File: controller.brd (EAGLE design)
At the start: 160 x 100 mm, 45 parts, among them IC1 MC34063AD, IC2 7805T, IC3 MEGA8-AI, Q1 IRF840, Q2 32768Hz, Q3 4MHz, T1 BC857, U1 DS1307Z

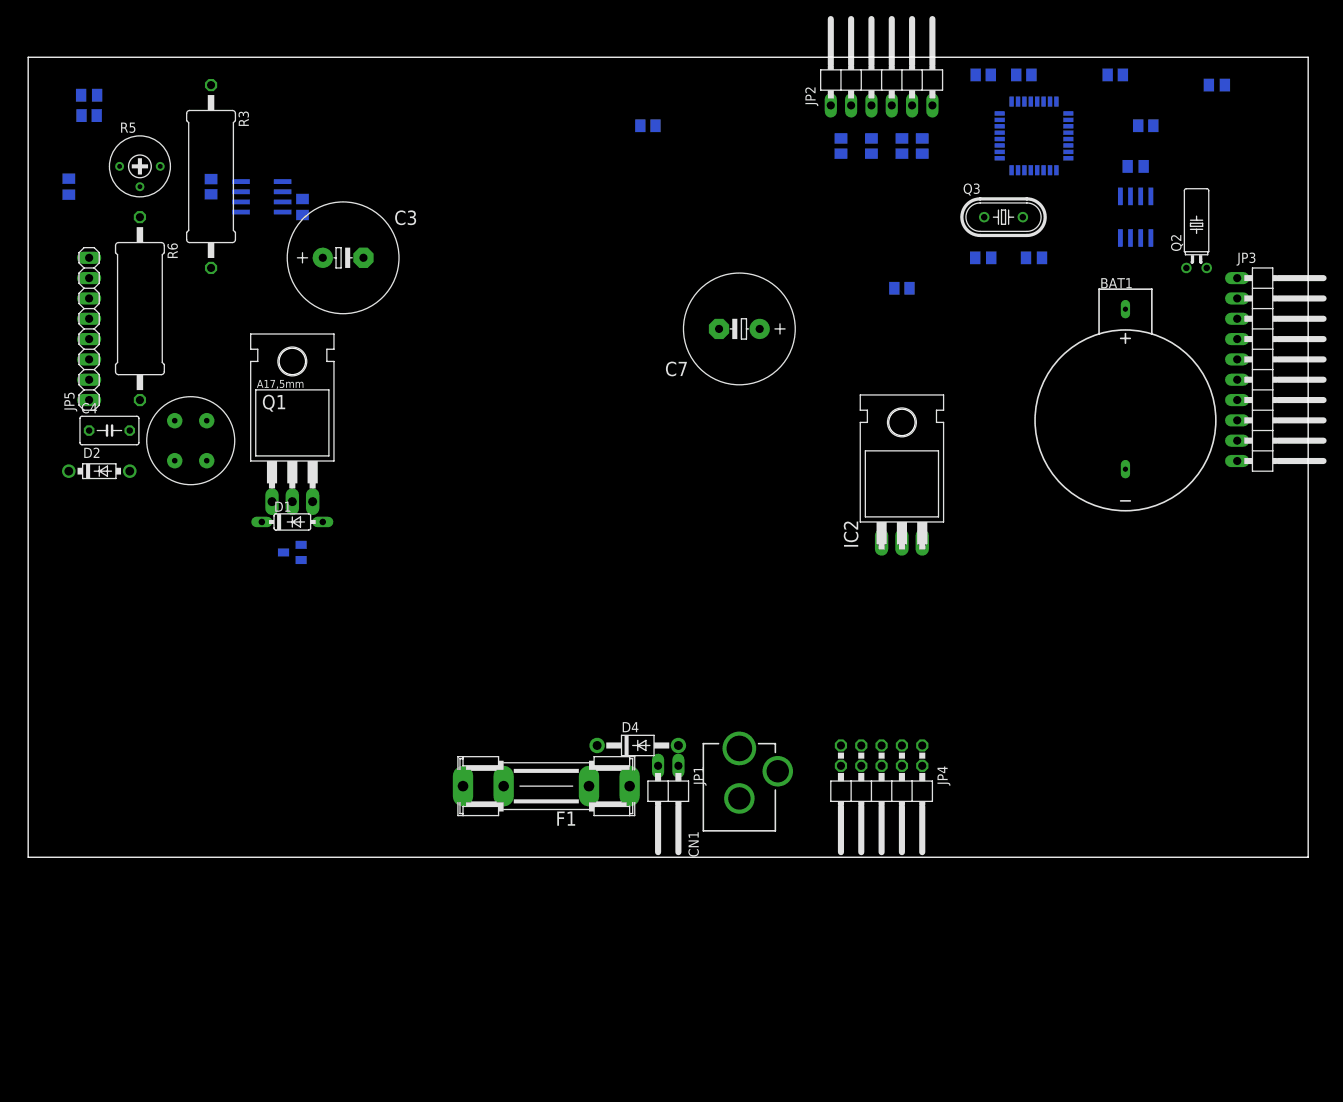
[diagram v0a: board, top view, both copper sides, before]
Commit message: Dimensions defined
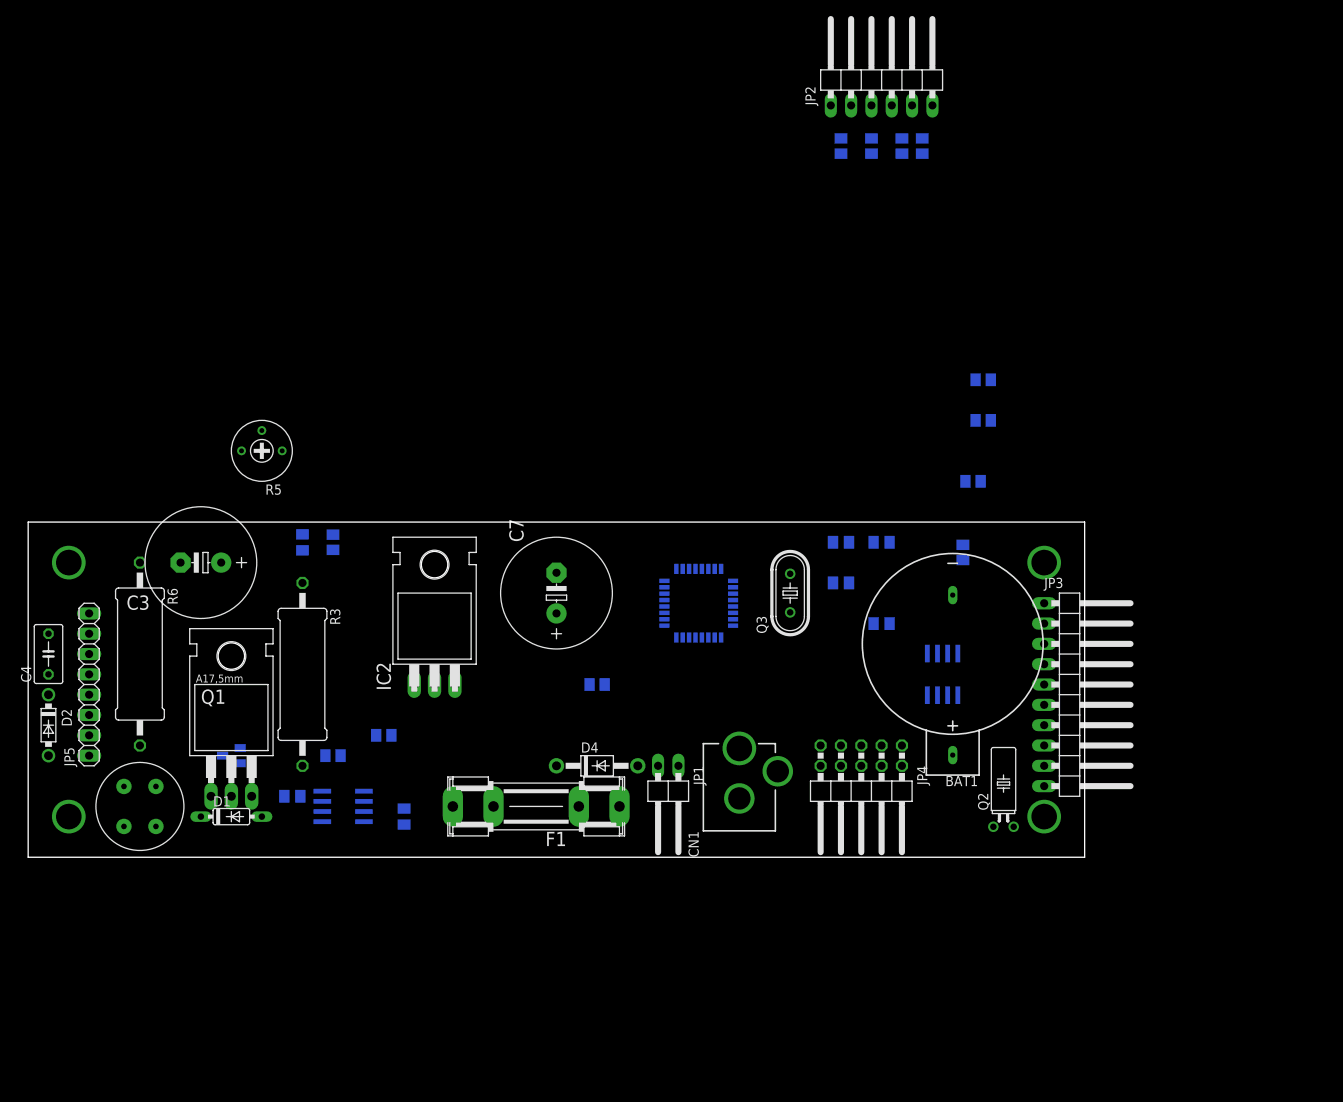
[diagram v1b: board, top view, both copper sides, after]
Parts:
- moved C2 91.2 mm to (33.0, 7.62)
- moved R1 83.0 mm to (44.5, 15.2)
- moved C1 77.3 mm to (47.0, 5.08)
- moved IC1 76.9 mm to (39.4, 6.35)
- moved Q2 73.9 mm to (121.9, 3.81)
- moved R2 72.7 mm to (38.1, 12.7), turned to 180 degrees
- moved IC3 71.9 mm to (83.8, 31.8)
- moved C5 70.9 mm to (106.7, 39.4), turned to 180 degrees
- moved C10 65.4 mm to (106.7, 29.2)
- moved R3 63.3 mm to (34.3, 22.9)
- moved R15 62.5 mm to (71.1, 21.6)
- moved U1 62.0 mm to (114.3, 22.9)
- moved R4 61.4 mm to (38.1, 39.4), turned to 90 degrees
- moved IC2 61.1 mm to (50.8, 31.8)
- moved R12 58.0 mm to (116.8, 38.1), turned to 90 degrees
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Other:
- board size 160 x 100 mm -> 132.1 x 41.9 mm

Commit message: Update
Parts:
- removed JP1: POWER +12V, pinhead:1X02/90
- removed JP3: EXTERNAL, pinhead:1X10/90
- moved C3 48.3 mm to (20.3, -11.4)
- moved JP2 47.2 mm to (78.7, 59.7)
- moved R10 47.2 mm to (83.8, 50.8)
- moved R8 47.2 mm to (77.5, 50.8)
- moved R9 47.2 mm to (81.3, 50.8)
- moved R7 46.5 mm to (74.9, 50.8)
- moved R5 43.0 mm to (15.2, 10.2)
- moved C6 34.9 mm to (53.3, 10.2), turned to 270 degrees
- moved R4 31.9 mm to (50.8, 10.2)
- moved D4 18.9 mm to (88.9, 17.8)
- moved R14 14.5 mm to (108.0, 50.8)
- moved R13 13.7 mm to (108.0, 47.0)
- moved R1 13.3 mm to (40.6, 2.54)
- moved Q1 11.5 mm to (24.1, 25.4)
- moved U$1 10.9 mm to (24.1, 10.2)
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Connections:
- removed net N$21: IC3.30, JP3.2
- removed net N$22: IC3.31, JP3.3
- removed net N$33: IC3.11, JP3.9
- removed net N$34: IC3.10, JP3.8
- removed net N$35: IC3.9, JP3.7
- removed net N$36: IC3.2, JP3.6
- removed net N$37: IC3.1, JP3.5
- net +5V: no longer JP3.1
- net GND: no longer JP1.1, JP3.10, JP3.4
- net N$29: no longer JP1.2

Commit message: .
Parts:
- added C11: 100nF, SparkFun-Passives:0805
- C1: value 200p -> 200pF; device resistor:C0805K -> SparkFun-Passives:0805
- C10, C2, C5, C6: value 100n -> 100nF; device resistor:C0805K -> SparkFun-Passives:0805
- C8, C9: device rcl:C0805K -> SparkFun-Passives:0805
- R1: value 1K -> 1k; device resistor:M0805 -> SparkFun-Passives:0805
- R10, R11, R12, R13, R14, R4, R7, R8, R9: value 10K -> 10k; device resistor:M0805 -> SparkFun-Passives:0805
- R15: value 1K -> 10k; device resistor:M0805 -> SparkFun-Passives:0805
- R3, R6: device resistor:0617/22 -> SparkFun-Passives:AXIAL-0.8
- moved C5 80.2 mm to (33.0, 7.62), flipped to the top
- moved C6 44.6 mm to (8.89, 6.35), flipped to the top, turned to 0 degrees
- moved R12 43.1 mm to (74.9, 48.3), flipped to the top, turned to 0 degrees
- moved R14 40.7 mm to (67.3, 48.3), flipped to the top, turned to 0 degrees
- moved R4 37.4 mm to (14.0, 3.81), flipped to the top, turned to 0 degrees
- moved R13 36.9 mm to (71.1, 48.3), flipped to the top, turned to 0 degrees
- moved R11 29.5 mm to (78.7, 48.3), flipped to the top, turned to 0 degrees
- moved C10 28.7 mm to (78.7, 22.9), flipped to the top, turned to 0 degrees
- moved R15 27.7 mm to (63.5, 48.3), flipped to the top
- moved C8 24.3 mm to (83.8, 22.9), flipped to the top
- moved R1 22.9 mm to (17.8, 3.81), flipped to the top
- moved C2 21.6 mm to (14.0, 1.27), flipped to the top, turned to 0 degrees
- moved R7 19.2 mm to (94.0, 48.3), flipped to the top, turned to 0 degrees
- moved C9 17.3 mm to (87.6, 24.1), flipped to the top
- moved R8 13.0 mm to (90.2, 48.3), flipped to the top, turned to 0 degrees
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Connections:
- net +5V: now also C6.1; no longer C5.1
- net 200V: now also R6.P$2; no longer R6.2
- net GND: now also C11.1
- net N$11: now also R6.P$1; no longer R6.1
- net N$18: now also R15.2; no longer R15.1
- net N$32: now also R15.1; no longer R15.2
- net N$7: now also R3.P$2; no longer R3.2
- net N$8: now also C5.1, R3.P$1; no longer C6.1, R3.1
- net N$9: now also C11.2

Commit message: .
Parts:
- moved R14 52.1 mm to (110.5, 19.1), flipped to the bottom, turned to 90 degrees
- moved R13 51.1 mm to (113.0, 19.1), flipped to the bottom, turned to 90 degrees
- moved R12 50.0 mm to (115.6, 19.1), flipped to the bottom, turned to 90 degrees
- moved JP2 44.7 mm to (115.6, 34.3)
- moved C10 40.7 mm to (119.4, 21.6), flipped to the bottom, turned to 180 degrees
- moved R10 39.6 mm to (119.4, 33.7), flipped to the bottom, turned to 90 degrees
- moved D1 35.3 mm to (43.2, 31.8), turned to 270 degrees
- moved R9 33.8 mm to (116.8, 33.7), flipped to the bottom, turned to 90 degrees
- moved R15 28.5 mm to (78.7, 24.1), flipped to the bottom, turned to 180 degrees
- moved R8 28.2 mm to (114.3, 33.7), flipped to the bottom, turned to 90 degrees
- moved D4 27.1 mm to (62.2, 12.7)
- moved F1 23.7 mm to (49.5, 5.08)
- moved R7 23.0 mm to (111.8, 33.7), flipped to the bottom, turned to 90 degrees
- moved Q2 16.5 mm to (128.3, 19.1), turned to 180 degrees
- moved BAT1 15.3 mm to (114.3, 11.4), turned to 0 degrees
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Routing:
- net +5V: track 0.00 -> 88.9 mm
- net N$24: track 0.00 -> 65.9 mm
- net N$30: track 0.00 -> 65.0 mm
- net N$31: track 0.00 -> 62.8 mm
- net N$32: track 0.00 -> 61.3 mm
- net GND: track 0.00 -> 45.3 mm
- net N$23: track 0.00 -> 17.3 mm
- net N$28: track 0.00 -> 9.25 mm
- net N$26: track 0.00 -> 7.98 mm
- net N$27: track 0.00 -> 3.78 mm
- net N$25: track 0.00 -> 3.11 mm
- net N$3: track 0.00 -> 2.28 mm
- net N$15: track 0.00 -> 2.28 mm
- net N$14: track 0.00 -> 2.28 mm
- net N$13: track 0.00 -> 2.28 mm

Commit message: Controller
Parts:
- removed R10, R7, R8, R9: 10k, SparkFun-Passives:0805
- C1: value 200pF -> 1nF
- C3: value 10u 450V -> 10uF 450V
- C4: value 100n 450V -> 100nF 450V; device resistor:C050-035X075 -> SparkFun-Passives:CAP-PTH-LARGE
- C7: value 470u -> 470uF
- R2: device resistor:M0805 -> SparkFun-Passives:0805
- moved C7 76.2 mm to (123.2, -21.6)
- moved C6 71.0 mm to (78.1, 22.2), flipped to the bottom
- moved C5 43.8 mm to (74.3, 22.2), flipped to the bottom
- moved R1 39.2 mm to (52.7, 21.6), flipped to the bottom, turned to 90 degrees
- moved C11 38.6 mm to (108.0, 10.2), turned to 270 degrees
- moved D2 38.1 mm to (36.2, 34.3), turned to 0 degrees
- moved C3 34.3 mm to (19.1, 22.9), turned to 0 degrees
- moved R11 32.3 mm to (108.0, 15.2), turned to 270 degrees
- moved T1 29.2 mm to (49.5, 21.6), flipped to the bottom, turned to 270 degrees
- moved IC2 25.5 mm to (76.2, 29.2)
- moved Q1 25.4 mm to (49.5, 24.1)
- moved R2 23.6 mm to (53.3, 5.08), turned to 90 degrees
- moved R3 20.8 mm to (47.0, 6.35), turned to 180 degrees
- moved F1 19.8 mm to (63.5, 19.1), turned to 90 degrees
- moved R4 19.7 mm to (33.7, 5.08), flipped to the bottom, turned to 90 degrees
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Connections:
- net +5V: no longer R10.2, R7.2, R8.2, R9.2
- net N$13: no longer R8.1
- net N$14: no longer R9.1
- net N$15: no longer R10.1
- net N$3: no longer R7.1
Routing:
- net GND: track 45.3 -> 289.2 mm
- net N$8: track 0.00 -> 56.1 mm
- net +5V: track 88.9 -> 144.2 mm
- net N$24: track 65.9 -> 118.8 mm
- net N$31: track 62.8 -> 115.6 mm
- net N$30: track 65.0 -> 117.2 mm
- net 200V: track 0.00 -> 43.4 mm
- net N$4: track 0.00 -> 33.2 mm
- net N$10: track 0.00 -> 32.6 mm, vias 0 -> 1
- net N$7: track 0.00 -> 27.5 mm
- net N$2: track 0.00 -> 26.2 mm
- net N$20: track 0.00 -> 25.2 mm, vias 0 -> 1
- net N$32: track 61.3 -> 86.0 mm
- net N$15: track 2.28 -> 20.9 mm
- net N$29: track 0.00 -> 18.5 mm
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- added copper zone on layer 16, net N$22

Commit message: .
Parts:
- moved Q2 3.59 mm to (125.7, 21.6), turned to 0 degrees
- moved R15 2.84 mm to (86.4, 33.0)
- moved C11 2.84 mm to (106.7, 12.7), turned to 90 degrees
- moved R11 1.80 mm to (106.7, 16.5), turned to 90 degrees
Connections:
- net N$25: now also Q2.1; no longer Q2.2
- net N$26: now also Q2.2; no longer Q2.1
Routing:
- net N$18: track 0.00 -> 34.0 mm, vias 0 -> 1
- net N$19: track 0.00 -> 26.5 mm, vias 0 -> 1
- net N$9: track 0.00 -> 26.1 mm
- net GND: track 289.2 -> 313.5 mm
- net N$32: track 86.0 -> 101.9 mm
- net +5V: track 144.2 -> 155.6 mm
- net N$26: track 7.98 -> 6.18 mm
- net N$20: track 25.2 -> 26.3 mm

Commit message: Controller prototype finished
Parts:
- removed C7: 470uF, resistor:E5-13
- added C12: 100uF, rcl:E3,5-8
- R5: value 200K -> (none); device resistor:RTRIM3339P -> rcl:RTRIM64Z
- moved C11 6.75 mm to (102.2, 17.8)
- moved R11 6.29 mm to (102.2, 21.0)
- moved R13 2.54 mm to (112.4, 15.2)
- moved R5 2.54 mm to (27.9, 7.62)
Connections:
- net +5V: now also C12.+; no longer C7.+
- net GND: now also C12.-; no longer C7.-
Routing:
- net +5V: track 155.6 -> 242.3 mm, vias 0 -> 3
- net GND: track 313.5 -> 342.7 mm
- net N$12: track 3.86 -> 27.8 mm, vias 0 -> 2
- net N$16: track 3.90 -> 24.4 mm
- net N$17: track 11.8 -> 19.1 mm, vias 0 -> 2
- net N$10: track 32.6 -> 39.0 mm, vias 1 -> 2
- net N$11: track 7.93 -> 14.1 mm
- net N$9: track 26.1 -> 30.5 mm
- net N$20: track 26.3 -> 25.2 mm
- net N$19: track 26.5 -> 25.9 mm
- net N$18: track 34.0 -> 33.4 mm
- removed copper zone on layer 16, net N$22

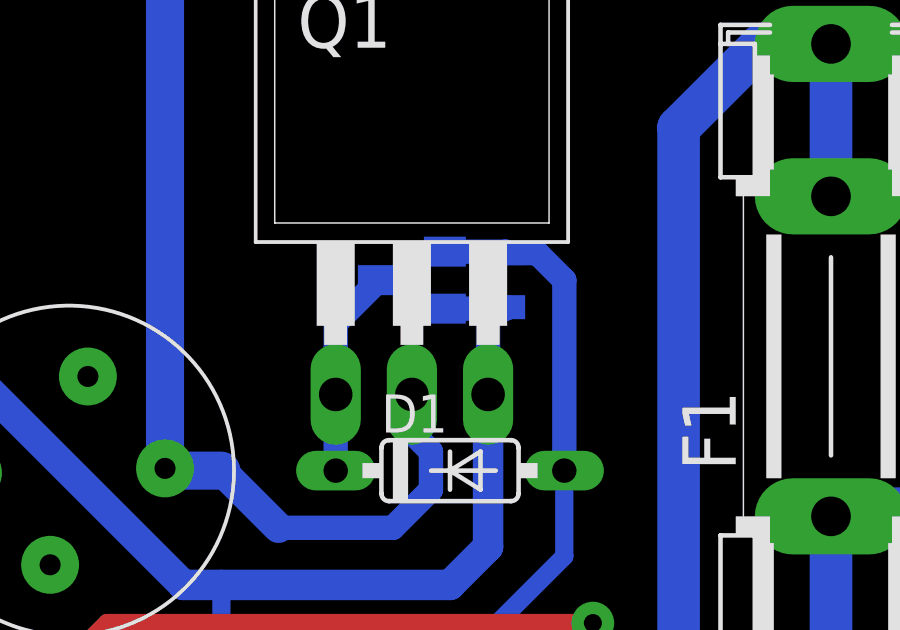
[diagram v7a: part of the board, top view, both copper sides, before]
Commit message: Correct pnp transistor pinout
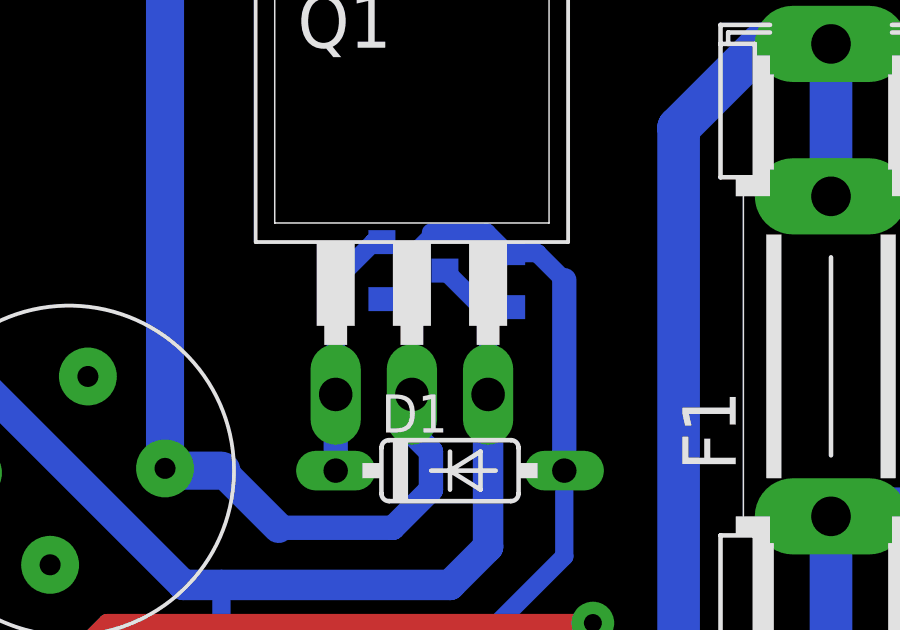
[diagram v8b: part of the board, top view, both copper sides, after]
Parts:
- removed T1: BC857, transistor:SOT23-BCE
- added Q6: BC857, SparkFun-DiscreteSemi:SOT23-3
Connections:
- net GND: now also Q6.3; no longer T1.C
- net N$1: now also Q6.2; no longer T1.E
- net N$2: now also Q6.1; no longer T1.B
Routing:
- net N$2: track 26.2 -> 30.3 mm
- net N$1: track 6.95 -> 8.42 mm
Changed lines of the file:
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@@
 </autorouter>
 <elements>
-<element name="T1" library="transistor" package="SOT23-BCE" value="BC857" x="49.53" y="21.59" rot="MR270"/>
 <element name="D1" library="diode" package="DO35-7" value="1N4148DO35-7" x="50.8" y="15.24"/>
 <element name="Q1" library="transistor-fet" package="TO220" value="IRF840" x="49.53" y="24.13"/>
@@
 <element name="C12" library="rcl" package="E3,5-8" value="100uF" x="85.725" y="18.415" rot="R270"/>
 <element name="R5" library="rcl" package="RTRIM64Z" value="" x="27.94" y="7.62" rot="R180"/>
+<element name="Q6" library="SparkFun-DiscreteSemi" package="SOT23-3" value="BC857" x="49.53" y="21.9075" rot="MR90"/>
 </elements>
 <signals>
 <signal name="N$1">
 <contactref element="D1" pad="C"/>
-<contactref element="T1" pad="E"/>
 <contactref element="Q1" pad="1"/>
-<wire x1="46.99" y1="17.78" x2="46.99" y2="20.15" width="0.8128" layer="16"/>
-<wire x1="46.99" y1="20.15" x2="48.43" y2="21.59" width="0.8128" layer="16"/>
 <wire x1="46.99" y1="17.78" x2="46.99" y2="15.24" width="0.8128" layer="16"/>
+<contactref element="Q6" pad="2"/>
+<wire x1="46.99" y1="17.78" x2="46.99" y2="21.59" width="0.6096" layer="16"/>
+<wire x1="46.99" y1="21.59" x2="48.26" y2="22.86" width="0.6096" layer="16"/>
+<wire x1="48.26" y1="22.86" x2="48.5275" y2="22.86" width="0.6096" layer="16"/>
+<wire x1="48.5275" y1="22.86" x2="48.53" y2="22.8575" width="0.6096" layer="16"/>
 </signal>
 <signal name="N$2">
 <contactref element="D1" pad="A"/>
-<contactref element="T1" pad="B"/>
 <contactref element="IC1" pad="2"/>
 <contactref element="R1" pad="2"/>
-<wire x1="50.63" y1="22.54" x2="52.655" y2="22.54" width="0.8128" layer="16"/>
-<wire x1="52.655" y1="22.54" x2="52.705" y2="22.49" width="0.8128" layer="16"/>
-<wire x1="52.705" y1="22.49" x2="53.71" y2="22.49" width="0.8128" layer="16"/>
-<wire x1="53.71" y1="22.49" x2="54.61" y2="21.59" width="0.8128" layer="16"/>
 <wire x1="54.61" y1="21.59" x2="54.61" y2="15.24" width="0.8128" layer="16"/>
 <wire x1="54.61" y1="15.24" x2="54.61" y2="12.3825" width="0.6096" layer="16"/>
@@
 <wire x1="46.99" y1="5.715" x2="48.26" y2="6.985" width="0.6096" layer="16"/>
 <wire x1="48.26" y1="6.985" x2="48.26" y2="8.5725" width="0.6096" layer="16"/>
+<contactref element="Q6" pad="1"/>
+<wire x1="48.53" y1="20.9575" x2="49.215" y2="20.9575" width="0.4064" layer="16"/>
+<wire x1="49.215" y1="20.9575" x2="49.53" y2="21.2725" width="0.4064" layer="16"/>
+<wire x1="49.53" y1="21.2725" x2="49.53" y2="22.5425" width="0.4064" layer="16"/>
+<wire x1="49.53" y1="22.5425" x2="50.165" y2="23.1775" width="0.4064" layer="16"/>
+<wire x1="52.705" y1="22.49" x2="53.71" y2="22.49" width="0.6096" layer="16"/>
+<wire x1="53.71" y1="22.49" x2="54.61" y2="21.59" width="0.6096" layer="16"/>
+<wire x1="50.165" y1="23.1775" x2="52.0175" y2="23.1775" width="0.6096" layer="16"/>
+<wire x1="52.0175" y1="23.1775" x2="52.705" y2="22.49" width="0.6096" layer="16"/>
 </signal>
 <signal name="N$5">
@@
 </signal>
 <signal name="GND">
-<contactref element="T1" pad="C"/>
 <contactref element="Q1" pad="3"/>
 <contactref element="IC1" pad="4"/>
@@
 <wire x1="21.59" y1="22.86" x2="24.13" y2="25.4" width="0.8128" layer="16"/>
 <wire x1="24.13" y1="25.4" x2="24.892" y2="25.4" width="0.8128" layer="16"/>
-<wire x1="50.63" y1="20.64" x2="52.07" y2="20.64" width="0.8128" layer="16"/>
-<wire x1="52.07" y1="20.64" x2="52.655" y2="20.64" width="0.8128" layer="16"/>
-<wire x1="52.655" y1="20.64" x2="52.705" y2="20.69" width="0.8128" layer="16"/>
-<wire x1="52.07" y1="17.78" x2="52.07" y2="20.64" width="0.8128" layer="16"/>
 <wire x1="43.18" y1="8.52" x2="44.185" y2="8.52" width="0.6096" layer="16"/>
 <wire x1="44.185" y1="8.52" x2="44.45" y2="8.255" width="0.6096" layer="16"/>
@@
 <wire x1="85.725" y1="10.115" x2="85.725" y2="15.24" width="1.27" layer="16"/>
 <wire x1="85.725" y1="15.24" x2="85.725" y2="16.637" width="1.27" layer="16"/>
+<contactref element="Q6" pad="3"/>
+<wire x1="52.07" y1="17.78" x2="52.07" y2="20.4675" width="0.6096" layer="16"/>
+<wire x1="52.07" y1="20.4675" x2="50.63" y2="21.9075" width="0.6096" layer="16"/>
+<wire x1="52.705" y1="20.69" x2="52.2925" y2="20.69" width="0.6096" layer="16"/>
+<wire x1="52.2925" y1="20.69" x2="52.07" y2="20.4675" width="0.6096" layer="16"/>
 </signal>
 <signal name="N$3">
